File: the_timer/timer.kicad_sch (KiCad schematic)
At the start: 23 parts, among them J1 AVR-ISP-6, J2 Conn_01x04_Socket, J3 Conn_01x02_Socket, Q1 2N7002, Q2 2N7002, Q3 2N7002, U1 ATtiny48-A, U2 TPS61033, U3 MC3416, U4 W25Q128JVS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

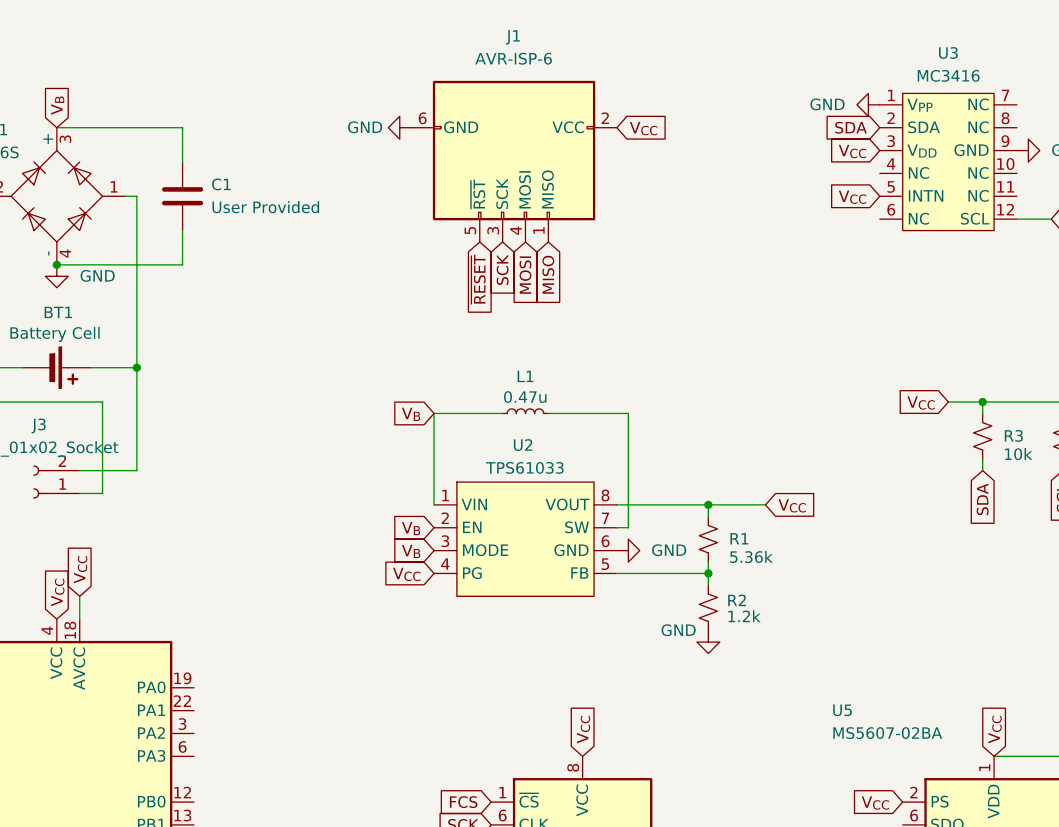
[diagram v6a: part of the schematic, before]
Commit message: Updated timer PCB
this might just be the worst board ever made
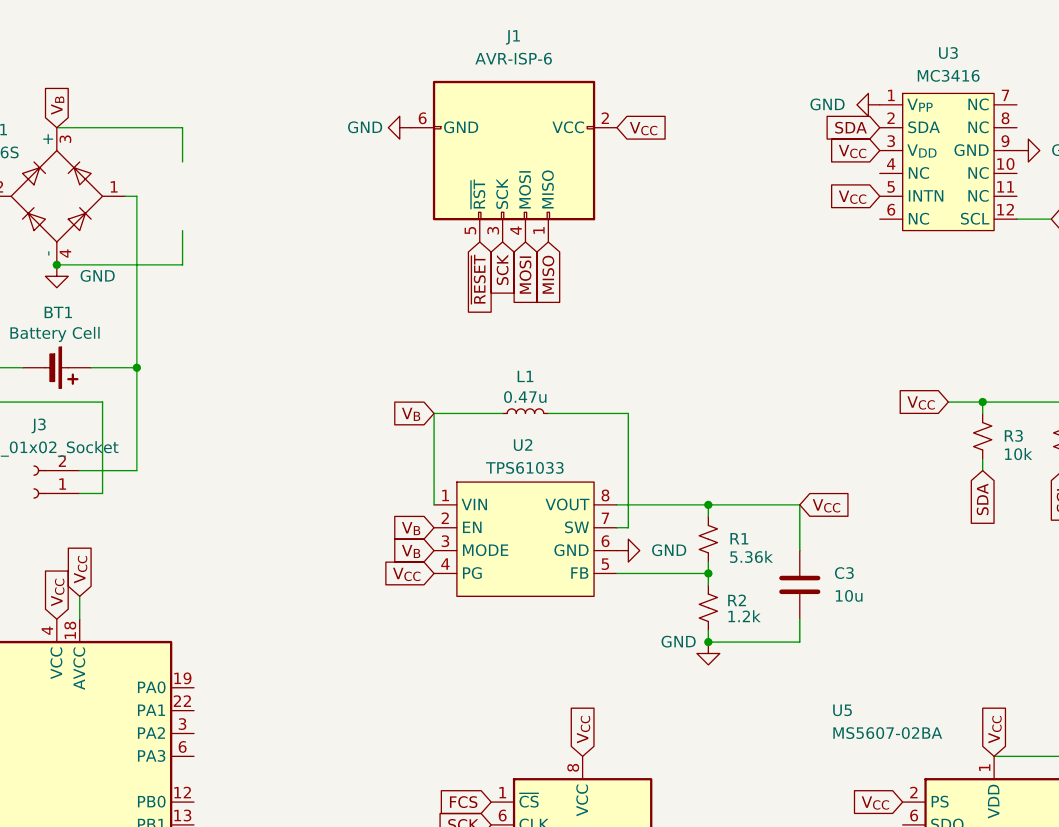
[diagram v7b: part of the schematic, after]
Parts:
- removed C1: User Provided, Connector_Wire:SolderWire-0.5sqmm_1x02_P4.8mm_D0.9mm_OD2.3mm, symbol Device:C
- added C3: 10u, Capacitor_SMD:C_0603_1608Metric, symbol Device:C
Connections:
- net GND: now also C3.2
- net V_{CC}: now also C3.1
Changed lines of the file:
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@@
 	)
 	(junction
+		(at 107.95 87.63)
+		(diameter 0)
+		(color 0 0 0 0)
+	)
+	(junction
 		(at 35.56 45.72)
 		(diameter 0)
@@
 	(wire
 		(pts
+			(xy 118.11 85.09) (xy 118.11 87.63)
+		)
+		(stroke
+			(width 0)
+			(type default)
+		)
+	)
+	(wire
+		(pts
 			(xy 85.09 62.23) (xy 77.47 62.23)
 		)
@@
 	(wire
 		(pts
+			(xy 118.11 72.39) (xy 118.11 77.47)
+		)
+		(stroke
+			(width 0)
+			(type default)
+		)
+	)
+	(wire
+		(pts
 			(xy 99.06 74.93) (xy 99.06 62.23)
 		)
@@
 	(wire
 		(pts
+			(xy 107.95 87.63) (xy 118.11 87.63)
+		)
+		(stroke
+			(width 0)
+			(type default)
+		)
+	)
+	(wire
+		(pts
 			(xy 49.53 30.48) (xy 49.53 34.29)
 		)
@@
 	(wire
 		(pts
-			(xy 107.95 72.39) (xy 114.3 72.39)
+			(xy 107.95 72.39) (xy 118.11 72.39)
 		)
 		(stroke
@@
 	(wire
 		(pts
+			(xy 107.95 87.63) (xy 107.95 86.36)
+		)
+		(stroke
+			(width 0)
+			(type default)
+		)
+	)
+	(wire
+		(pts
 			(xy 39.37 57.15) (xy 44.45 57.15)
 		)
@@
 	(global_label "V_{CC}"
 		(shape input)
-		(at 114.3 72.39 0)
+		(at 118.11 72.39 0)
 		(fields_autoplaced yes)
 		(effects
@@
 		)
 		(property "Intersheetrefs" "${INTERSHEET_REFS}"
-			(at 120.4566 72.39 0)
+			(at 124.2666 72.39 0)
 			(effects
 				(font
@@
 	)
 	(symbol
-		(lib_id "Device:C")
-		(at 49.53 38.1 0)
-		(unit 1)
-		(exclude_from_sim no)
-		(in_bom yes)
-		(on_board yes)
-		(dnp no)
-		(fields_autoplaced yes)
-		(property "Reference" "C1"
-			(at 52.705 36.83 0)
-			(effects
-				(font
-					(size 1.27 1.27)
-				)
-				(justify left)
-			)
-		)
-		(property "Value" "User Provided"
-			(at 52.705 39.37 0)
-			(effects
-				(font
-					(size 1.27 1.27)
-				)
-				(justify left)
-			)
-		)
-		(property "Footprint" "Connector_Wire:SolderWire-0.5sqmm_1x02_P4.8mm_D0.9mm_OD2.3mm"
-			(at 50.4952 41.91 0)
-			(effects
-				(font
-					(size 1.27 1.27)
-				)
-				(hide yes)
-			)
-		)
-		(property "Datasheet" "~"
-			(at 49.53 38.1 0)
-			(effects
-				(font
-					(size 1.27 1.27)
-				)
-				(hide yes)
-			)
-		)
-		(property "Description" "User Provided, ~220u"
-			(at 49.53 38.1 0)
-			(effects
-				(font
-					(size 1.27 1.27)
-				)
-				(hide yes)
-			)
-		)
-		(property "DKPN" ""
-			(at 49.53 38.1 0)
-			(effects
-				(font
-					(size 1.27 1.27)
-				)
-				(hide yes)
-			)
-		)
-		(pin "1"
-		)
-		(pin "2"
-		)
-		(instances
-			(project "timer"
-				(path "/e2b0a296-fcac-4dcc-93f1-26b3dc1147d1"
-					(reference "C1")
-					(unit 1)
-				)
-			)
-			(project "Ping"
-				(path "/fd9615be-e2a3-47ef-8586-c415f6857bc8"
-					(reference "C2")
-					(unit 1)
-				)
-			)
-		)
-	)
-	(symbol
 		(lib_name "GND_1")
 		(lib_id "power:GND")
@@
 	)
 	(symbol
+		(lib_id "Device:C")
+		(at 118.11 81.28 0)
+		(unit 1)
+		(exclude_from_sim no)
+		(in_bom yes)
+		(on_board yes)
+		(dnp no)
+		(fields_autoplaced yes)
+		(property "Reference" "C3"
+			(at 121.92 80.0099 0)
+			(effects
+				(font
+					(size 1.27 1.27)
+				)
+				(justify left)
+			)
+		)
+		(property "Value" "10u"
+			(at 121.92 82.5499 0)
+			(effects
+				(font
+					(size 1.27 1.27)
+				)
+				(justify left)
+			)
+		)
+		(property "Footprint" "Capacitor_SMD:C_0603_1608Metric"
+			(at 119.0752 85.09 0)
+			(effects
+				(font
+					(size 1.27 1.27)
+				)
+				(hide yes)
+			)
+		)
+		(property "Datasheet" "~"
+			(at 118.11 81.28 0)
+			(effects
+				(font
+					(size 1.27 1.27)
+				)
+				(hide yes)
+			)
+		)
+		(property "Description" ""
+			(at 118.11 81.28 0)
+			(effects
+				(font
+					(size 1.27 1.27)
+				)
+				(hide yes)
+			)
+		)
+		(property "DKPN" "490-12538-1-ND"
+			(at 118.11 81.28 0)
+			(effects
+				(font
+					(size 1.27 1.27)
+				)
+				(hide yes)
+			)
+		)
+		(pin "1"
+		)
+		(pin "2"
+		)
+		(instances
+			(project "timer"
+				(path "/e2b0a296-fcac-4dcc-93f1-26b3dc1147d1"
+					(reference "C3")
+					(unit 1)
+				)
+			)
+		)
+	)
+	(symbol
 		(lib_id "Device:Battery_Cell")
 		(at 34.29 57.15 270)
@@
 	(symbol
 		(lib_id "power:GND")
-		(at 107.95 86.36 0)
+		(at 107.95 87.63 0)
 		(unit 1)
 		(exclude_from_sim no)
@@
 		(dnp no)
 		(property "Reference" "#PWR010"
-			(at 107.95 92.71 0)
+			(at 107.95 93.98 0)
 			(effects
 				(font
@@
 		)
 		(property "Value" "GND"
-			(at 104.648 86.36 0)
+			(at 104.648 87.63 0)
 			(effects
 				(font
@@
 		)
 		(property "Footprint" ""
-			(at 107.95 86.36 0)
+			(at 107.95 87.63 0)
 			(effects
 				(font
@@
 		)
 		(property "Datasheet" ""
-			(at 107.95 86.36 0)
+			(at 107.95 87.63 0)
 			(effects
 				(font
@@
 		)
 		(property "Description" ""
-			(at 107.95 86.36 0)
+			(at 107.95 87.63 0)
 			(effects
 				(font

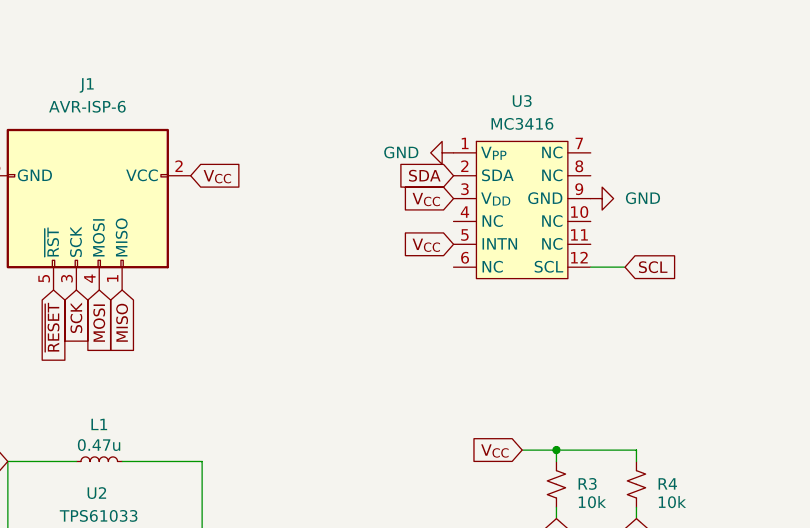
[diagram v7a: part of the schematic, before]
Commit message: Added datasheets to Timer schematic
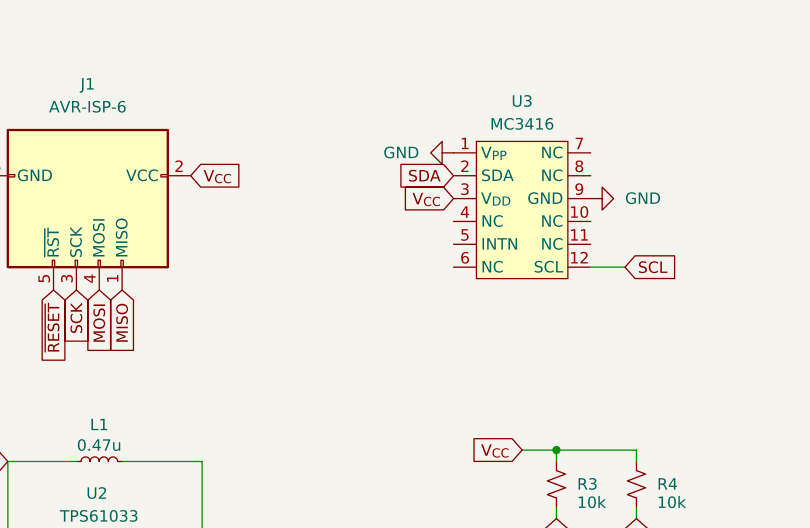
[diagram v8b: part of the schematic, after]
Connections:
- net V_{CC}: no longer U3.5 (INTN)
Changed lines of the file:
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@@
-		)
-	)
-	(global_label "V_{CC}"
-		(shape input)
-		(at 127 38.1 180)
-		(fields_autoplaced yes)
-		(effects
-			(font
-				(size 1.27 1.27)
-			)
-			(justify right)
-		)
-		(property "Intersheetrefs" "${INTERSHEET_REFS}"
-			(at 120.8434 38.1 0)
-			(effects
-				(font
-					(size 1.27 1.27)
-				)
-				(justify right)
-				(hide yes)
-			)
 		)
 	)
@@
 			)
 		)
-		(property "Datasheet" ""
+		(property "Datasheet" "https://www.memsic.com/Public/Uploads/uploadfile/files/20220522/MC3416Datasheet(APS-045-0020v2.2).pdf"
 			(at 134.62 35.56 0)
 			(effects
